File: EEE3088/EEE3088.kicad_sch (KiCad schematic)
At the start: 0 parts

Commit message: Power update
included Low voltage reg
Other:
- company: (none) -> UCT
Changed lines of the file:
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@@
 (kicad_sch (version 20230121) (generator eeschema)
   (paper "A4")
+  (title_block
+    (company "UCT")
+  )
   (sheet (at 40.64 48.26) (size 30.48 19.05) (fields_autoplaced)
     (stroke (width 0.1524) (type solid))

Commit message: Rev_1_compl.
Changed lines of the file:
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@@
     (company "UCT")
   )
-  (sheet (at 40.64 48.26) (size 30.48 19.05) (fields_autoplaced)
+  (hierarchical_label "LDR_Vout_1" (shape input) (at 200.66 90.17 0) (fields_autoplaced)
+    (effects (font (size 1.27 1.27)) (justify left))
+  )
+  (hierarchical_label "LDR_Vout_2" (shape input) (at 200.66 92.71 0) (fields_autoplaced)
+    (effects (font (size 1.27 1.27)) (justify left))
+  )
+  (hierarchical_label "SDA_Sense" (shape input) (at 200.66 86.36 0) (fields_autoplaced)
+    (effects (font (size 1.27 1.27)) (justify left))
+  )
+  (hierarchical_label "SCL_Sense" (shape input) (at 200.66 83.82 0) (fields_autoplaced)
+    (effects (font (size 1.27 1.27)) (justify left))
+  )
+  (sheet (at 80.01 80.01) (size 26.67 20.32) (fields_autoplaced)
     (stroke (width 0.1524) (type solid))
     (fill (color 0 0 0 0.0000))
-    (property "Sheetname" "Power_Subsystem" (at 40.64 47.5484 0)
+    (property "Sheetname" "Power_Subsystem" (at 80.01 79.2984 0)
       (effects (font (size 1.27 1.27)) (justify left bottom))
     )
-    (property "Sheetfile" "Power_kicad_sch.kicad_sch" (at 40.64 67.8946 0)
+    (property "Sheetfile" "Power_kicad_sch.kicad_sch" (at 80.01 100.9146 0)
       (effects (font (size 1.27 1.27)) (justify left top))
     )
@@
     )
   )
-  (sheet (at 48.26 80.01) (size 41.91 25.4) (fields_autoplaced)
+  (sheet (at 143.51 80.01) (size 26.67 20.32) (fields_autoplaced)
     (stroke (width 0.1524) (type solid))
     (fill (color 0 0 0 0.0000))
-    (property "Sheetname" "Microcontroller" (at 48.26 79.2984 0)
+    (property "Sheetname" "Microcontroller" (at 143.51 79.2984 0)
       (effects (font (size 1.27 1.27)) (justify left bottom))
     )
-    (property "Sheetfile" "Microcontroller_kicad_sch.kicad_sch" (at 48.26 105.9946 0)
+    (property "Sheetfile" "Microcontroller_kicad_sch.kicad_sch" (at 143.51 100.9146 0)
       (effects (font (size 1.27 1.27)) (justify left top))
     )
@@
     )
   )
-  (sheet (at 105.41 50.8) (size 45.72 17.78) (fields_autoplaced)
+  (sheet (at 200.66 80.01) (size 26.67 20.32) (fields_autoplaced)
     (stroke (width 0.1524) (type solid))
     (fill (color 0 0 0 0.0000))
-    (property "Sheetname" "Sensing_Subsystem" (at 105.41 50.0884 0)
+    (property "Sheetname" "Sensing_Subsystem" (at 200.66 79.2984 0)
       (effects (font (size 1.27 1.27)) (justify left bottom))
     )
-    (property "Sheetfile" "Sensing_kicad_sch.kicad_sch" (at 105.41 69.1646 0)
+    (property "Sheetfile" "Sensing_kicad_sch.kicad_sch" (at 200.66 100.9146 0)
       (effects (font (size 1.27 1.27)) (justify left top))
     )

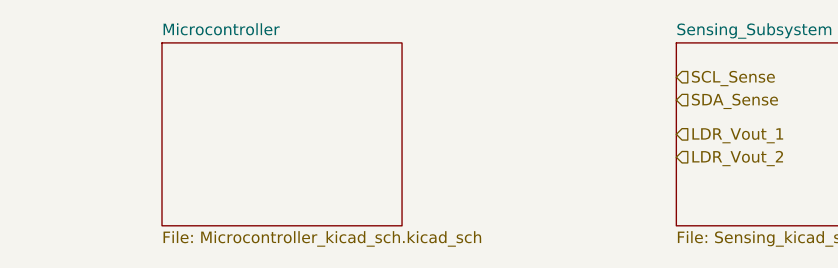
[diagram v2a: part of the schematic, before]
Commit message: better microcontroller sheet
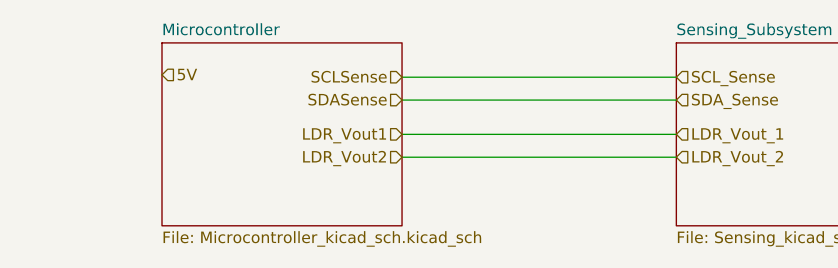
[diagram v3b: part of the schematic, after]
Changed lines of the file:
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@@
     (company "UCT")
   )
+  (wire (pts (xy 170.18 92.71) (xy 200.66 92.71))
+    (stroke (width 0) (type default))
+  )
+  (wire (pts (xy 170.18 86.36) (xy 200.66 86.36))
+    (stroke (width 0) (type default))
+  )
+  (wire (pts (xy 170.18 83.82) (xy 200.66 83.82))
+    (stroke (width 0) (type default))
+  )
+  (wire (pts (xy 170.18 90.17) (xy 200.66 90.17))
+    (stroke (width 0) (type default))
+  )
   (hierarchical_label "LDR_Vout_1" (shape input) (at 200.66 90.17 0) (fields_autoplaced)
+    (effects (font (size 1.27 1.27)) (justify left))
+  )
+  (hierarchical_label "SCLSense" (shape input) (at 170.18 83.82 180) (fields_autoplaced)
+    (effects (font (size 1.27 1.27)) (justify right))
+  )
+  (hierarchical_label "LDR_Vout2" (shape input) (at 170.18 92.71 180) (fields_autoplaced)
+    (effects (font (size 1.27 1.27)) (justify right))
+  )
+  (hierarchical_label "5V" (shape input) (at 143.51 83.566 0) (fields_autoplaced)
     (effects (font (size 1.27 1.27)) (justify left))
   )
@@
     (effects (font (size 1.27 1.27)) (justify left))
   )
+  (hierarchical_label "LDR_Vout1" (shape input) (at 170.18 90.17 180) (fields_autoplaced)
+    (effects (font (size 1.27 1.27)) (justify right))
+  )
   (hierarchical_label "SDA_Sense" (shape input) (at 200.66 86.36 0) (fields_autoplaced)
     (effects (font (size 1.27 1.27)) (justify left))
   )
+  (hierarchical_label "SDASense" (shape input) (at 170.18 86.36 180) (fields_autoplaced)
+    (effects (font (size 1.27 1.27)) (justify right))
+  )
   (hierarchical_label "SCL_Sense" (shape input) (at 200.66 83.82 0) (fields_autoplaced)

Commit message: Sense_V1_Submission
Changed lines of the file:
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@@
     (company "UCT")
+  )
+  (wire (pts (xy 95.25 137.16) (xy 90.17 137.16))
+    (stroke (width 0) (type default))
   )
   (wire (pts (xy 170.18 92.71) (xy 200.66 92.71))
@@
   (wire (pts (xy 170.18 90.17) (xy 200.66 90.17))
     (stroke (width 0) (type default))
+  )
+  (wire (pts (xy 95.25 133.35) (xy 95.25 137.16))
+    (stroke (width 0) (type default))
+  )
+  (global_label "+3.3V" (shape output) (at 90.17 137.16 180) (fields_autoplaced)
+    (effects (font (size 1.27 1.27)) (justify right))
+    (property "Intersheetrefs" "${INTERSHEET_REFS}" (at 81.5794 137.16 0)
+      (effects (font (size 1.27 1.27)) (justify right) hide)
+    )
   )
   (hierarchical_label "LDR_Vout_1" (shape input) (at 200.66 90.17 0) (fields_autoplaced)
@@
     (effects (font (size 1.27 1.27)) (justify left))
   )
+  (symbol (lib_id "power:+3.3V") (at 95.25 133.35 0) (unit 1)
+    (in_bom yes) (on_board yes) (dnp no) (fields_autoplaced)
+    (property "Reference" "#PWR044" (at 95.25 137.16 0)
+      (effects (font (size 1.27 1.27)) hide)
+    )
+    (property "Value" "+3.3V" (at 95.25 129.54 0)
+      (effects (font (size 1.27 1.27)))
+    )
+    (property "Footprint" "" (at 95.25 133.35 0)
+      (effects (font (size 1.27 1.27)) hide)
+    )
+    (property "Datasheet" "" (at 95.25 133.35 0)
+      (effects (font (size 1.27 1.27)) hide)
+    )
+    (pin "1")
+    (instances
+      (project "EEE3088"
+        (path "/83bdd5e1-981a-4ca1-9a2f-70dea9f00850/d16a673b-d677-4a4a-a11c-ee22bd422692"
+          (reference "#PWR044") (unit 1)
+        )
+        (path "/83bdd5e1-981a-4ca1-9a2f-70dea9f00850"
+          (reference "#PWR027") (unit 1)
+        )
+      )
+    )
+  )
   (sheet (at 80.01 80.01) (size 26.67 20.32) (fields_autoplaced)

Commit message: power edit
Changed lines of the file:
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@@
     (company "UCT")
   )
+  (junction (at 133.985 94.615) (diameter 0) (color 0 0 0 0)
+  )
+  (wire (pts (xy 133.985 94.615) (xy 143.51 94.615))
+    (stroke (width 0) (type default))
+  )
   (wire (pts (xy 95.25 137.16) (xy 90.17 137.16))
+    (stroke (width 0) (type default))
+  )
+  (wire (pts (xy 133.985 105.41) (xy 193.675 105.41))
+    (stroke (width 0) (type default))
+  )
+  (wire (pts (xy 106.68 94.615) (xy 133.985 94.615))
     (stroke (width 0) (type default))
   )
@@
     (stroke (width 0) (type default))
   )
+  (wire (pts (xy 193.675 105.41) (xy 193.675 96.52))
+    (stroke (width 0) (type default))
+  )
   (wire (pts (xy 170.18 86.36) (xy 200.66 86.36))
+    (stroke (width 0) (type default))
+  )
+  (wire (pts (xy 133.985 94.615) (xy 133.985 105.41))
     (stroke (width 0) (type default))
   )
@@
     (stroke (width 0) (type default))
   )
+  (wire (pts (xy 106.68 83.82) (xy 143.51 83.82))
+    (stroke (width 0) (type default))
+  )
+  (wire (pts (xy 193.675 96.52) (xy 200.66 96.52))
+    (stroke (width 0) (type default))
+  )
   (global_label "+3.3V" (shape output) (at 90.17 137.16 180) (fields_autoplaced)
     (effects (font (size 1.27 1.27)) (justify right))
@@
     (effects (font (size 1.27 1.27)) (justify left))
   )
+  (hierarchical_label "+3.3V" (shape input) (at 200.66 96.52 0) (fields_autoplaced)
+    (effects (font (size 1.27 1.27)) (justify left))
+  )
   (hierarchical_label "SCLSense" (shape input) (at 170.18 83.82 180) (fields_autoplaced)
     (effects (font (size 1.27 1.27)) (justify right))
@@
     (effects (font (size 1.27 1.27)) (justify right))
   )
-  (hierarchical_label "5V" (shape input) (at 143.51 83.566 0) (fields_autoplaced)
+  (hierarchical_label "+3.3V" (shape input) (at 106.68 94.615 180) (fields_autoplaced)
+    (effects (font (size 1.27 1.27)) (justify right))
+  )
+  (hierarchical_label "+3.3V" (shape input) (at 143.51 94.615 0) (fields_autoplaced)
+    (effects (font (size 1.27 1.27)) (justify left))
+  )
+  (hierarchical_label "5V" (shape input) (at 143.51 83.82 0) (fields_autoplaced)
     (effects (font (size 1.27 1.27)) (justify left))
   )
   (hierarchical_label "LDR_Vout_2" (shape input) (at 200.66 92.71 0) (fields_autoplaced)
     (effects (font (size 1.27 1.27)) (justify left))
+  )
+  (hierarchical_label "5V" (shape input) (at 106.68 83.82 180) (fields_autoplaced)
+    (effects (font (size 1.27 1.27)) (justify right))
   )
   (hierarchical_label "LDR_Vout1" (shape input) (at 170.18 90.17 180) (fields_autoplaced)
@@
         )
         (path "/83bdd5e1-981a-4ca1-9a2f-70dea9f00850"
-          (reference "#PWR027") (unit 1)
+          (reference "#PWR01") (unit 1)
         )
       )
